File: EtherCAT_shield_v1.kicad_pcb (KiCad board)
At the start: 2 copper layers, 73.7 x 81.3 mm, 105 parts, among them J1 RJ45-PULSETRANS, J2 RJ45-PULSETRANS, J3 GS3, J4 GS3, J5 GS3, J6 GS3, J7 GS2, J8 GS2, P1 CONN_02X10, P2 CONN_02X19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

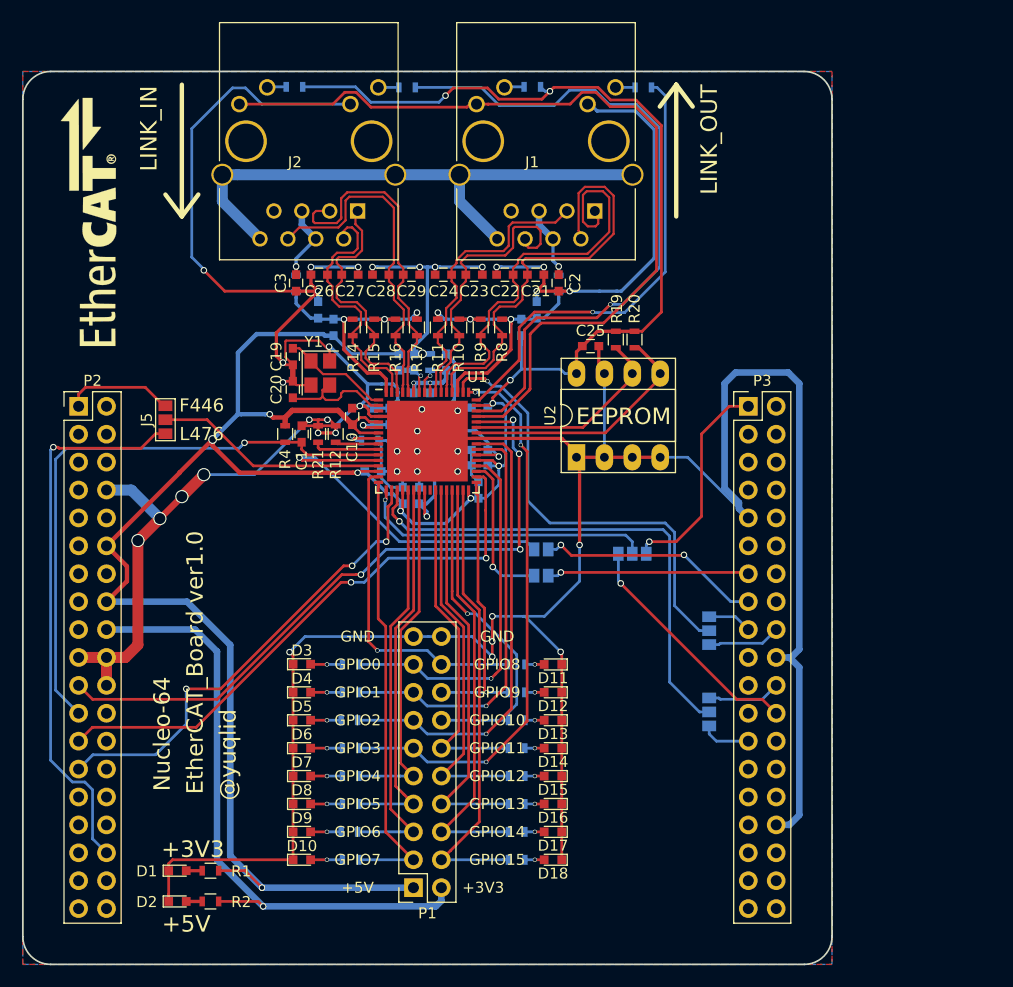
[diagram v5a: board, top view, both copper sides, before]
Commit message: 外形を変更
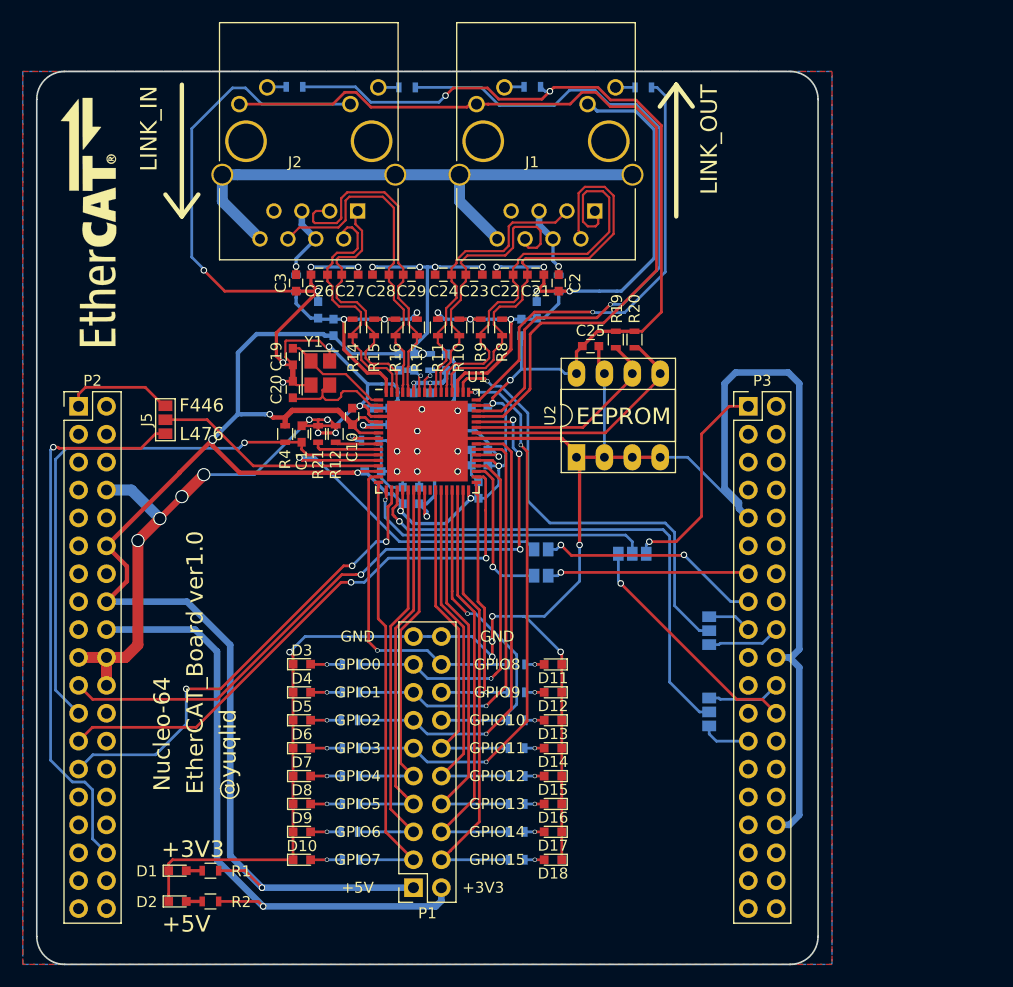
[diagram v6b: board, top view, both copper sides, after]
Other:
- board size 73.7 x 81.3 mm -> 71.1 x 81.3 mm
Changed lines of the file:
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@@
-(kicad_pcb (version 4) (host pcbnew 4.0.6)
+(kicad_pcb (version 4) (host pcbnew 4.0.5)
   (general
     (links 268)
@@
   )
   (setup
-    (last_trace_width 0.4)
+    (last_trace_width 0.25)
     (user_trace_width 0.2)
     (user_trace_width 0.3)
@@
     )
   )
-  (gr_arc (start 99.06 53.34) (end 96.52 53.34) (angle 90) (layer Edge.Cuts) (width 0.15))
-  (gr_arc (start 167.64 53.34) (end 167.64 50.8) (angle 90) (layer Edge.Cuts) (width 0.15))
+  (gr_arc (start 100.33 53.34) (end 97.79 53.34) (angle 90) (layer Edge.Cuts) (width 0.15))
+  (gr_arc (start 166.37 53.34) (end 166.37 50.8) (angle 90) (layer Edge.Cuts) (width 0.15))
   (gr_text EEPROM (at 151.2 82.2) (layer F.SilkS)
     (effects (font (size 1.5 1.5) (thickness 0.3)))
@@
   (gr_line (start 146 93) (end 139.8 93) (layer B.SilkS) (width 0.2))
   (gr_line (start 146 98) (end 146 93) (layer B.SilkS) (width 0.2))
-  (gr_text L476 (at 142.8 98.8 360) (layer B.SilkS)
+  (gr_text L476 (at 142.8 98.8) (layer B.SilkS)
     (effects (font (size 1.2 1.2) (thickness 0.2)) (justify mirror))
   )
@@
     (effects (font (size 1.5 1.5) (thickness 0.3)))
   )
-  (gr_arc (start 99.06 129.54) (end 99.06 132.08) (angle 90) (layer Edge.Cuts) (width 0.15))
-  (gr_arc (start 167.64 129.54) (end 170.18 129.54) (angle 90) (layer Edge.Cuts) (width 0.15))
-  (gr_line (start 170.18 53.34) (end 170.18 129.54) (layer Edge.Cuts) (width 0.15))
-  (gr_line (start 99.06 50.8) (end 167.64 50.8) (layer Edge.Cuts) (width 0.15))
-  (gr_line (start 96.52 129.54) (end 96.52 53.34) (layer Edge.Cuts) (width 0.15))
-  (gr_line (start 167.64 132.08) (end 99.06 132.08) (layer Edge.Cuts) (width 0.15))
+  (gr_arc (start 100.33 129.54) (end 100.33 132.08) (angle 90) (layer Edge.Cuts) (width 0.15))
+  (gr_arc (start 166.37 129.54) (end 168.91 129.54) (angle 90) (layer Edge.Cuts) (width 0.15))
+  (gr_line (start 168.91 53.34) (end 168.91 129.54) (layer Edge.Cuts) (width 0.15))
+  (gr_line (start 100.33 50.8) (end 166.37 50.8) (layer Edge.Cuts) (width 0.15))
+  (gr_line (start 97.79 129.54) (end 97.79 53.34) (layer Edge.Cuts) (width 0.15))
+  (gr_line (start 166.37 132.08) (end 100.33 132.08) (layer Edge.Cuts) (width 0.15))
   (segment (start 119.6 74.6) (end 119.6 76.7) (width 0.3) (layer F.Cu) (net 1))
   (segment (start 119.6 76.7) (end 120.2 77.3) (width 0.3) (layer F.Cu) (net 1))
@@
     (connect_pads (clearance 0.254))
     (min_thickness 0.254)
-    (fill yes (arc_segments 16) (thermal_gap 0.508) (thermal_bridge_width 0.508))
+    (fill (arc_segments 16) (thermal_gap 0.508) (thermal_bridge_width 0.508))
     (polygon
       (pts
@@
     (connect_pads (clearance 0.254))
     (min_thickness 0.254)
-    (fill yes (arc_segments 16) (thermal_gap 0.508) (thermal_bridge_width 0.508))
+    (fill (arc_segments 16) (thermal_gap 0.508) (thermal_bridge_width 0.508))
     (polygon
       (pts
@@
     (min_thickness 0.254)
     (keepout (tracks not_allowed) (vias not_allowed) (copperpour not_allowed))
-    (fill yes (arc_segments 16) (thermal_gap 0.508) (thermal_bridge_width 0.508))
+    (fill (arc_segments 16) (thermal_gap 0.508) (thermal_bridge_width 0.508))
     (polygon
       (pts
@@
     (min_thickness 0.254)
     (keepout (tracks not_allowed) (vias not_allowed) (copperpour not_allowed))
-    (fill yes (arc_segments 16) (thermal_gap 0.508) (thermal_bridge_width 0.508))
+    (fill (arc_segments 16) (thermal_gap 0.508) (thermal_bridge_width 0.508))
     (polygon
       (pts

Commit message: 外形線を変更
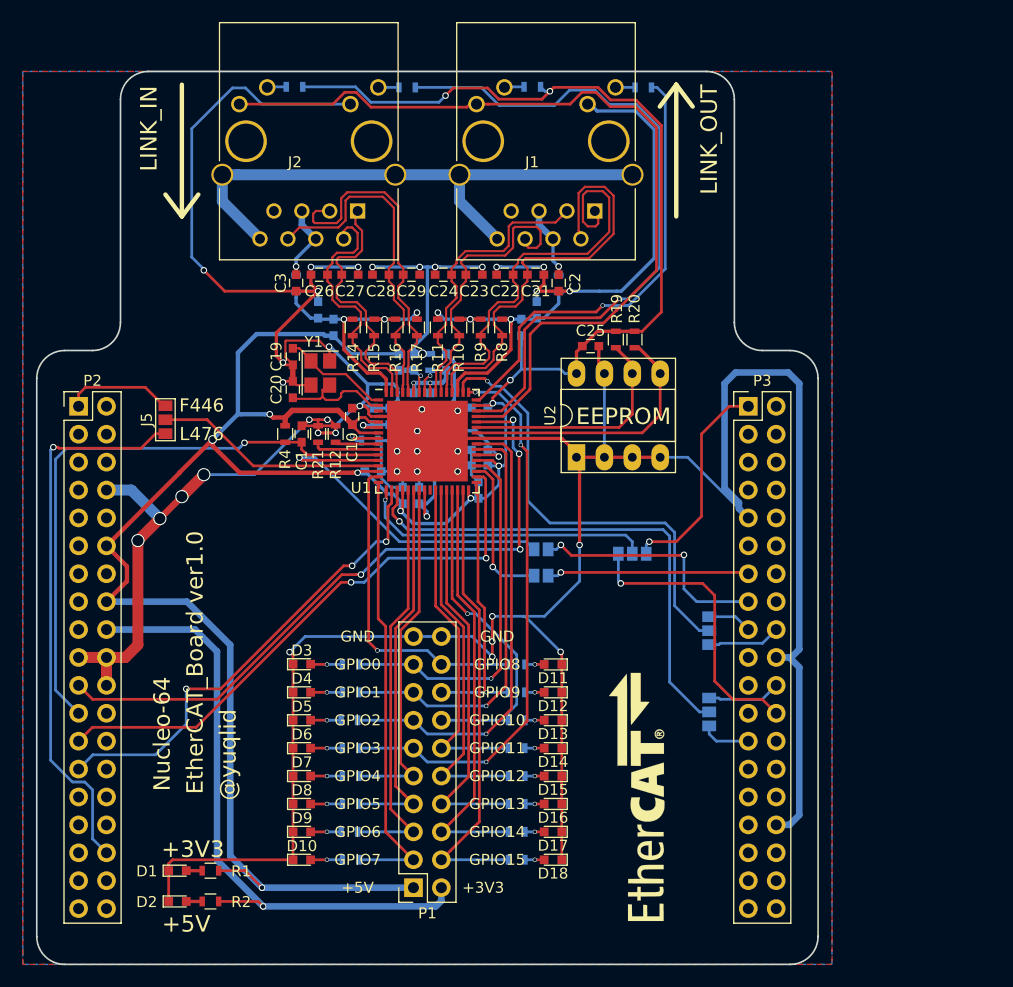
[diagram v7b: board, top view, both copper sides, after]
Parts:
- moved G*** 72.3 mm to (152.4, 116.8)
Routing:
- net PB1: track 21.6 -> 26.4 mm
- net Net-(R20-Pad2): track 22.8 -> 24.7 mm
- net Net-(R19-Pad2): track 19.5 -> 21.4 mm
- net PA7: track 20.6 -> 22.4 mm
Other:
- outline, holes or cut-outs redrawn
